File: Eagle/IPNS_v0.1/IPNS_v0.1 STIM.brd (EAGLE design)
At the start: 32.9 x 17.8 mm, 21 parts, among them J1 OUTPUT CONN, J2 POL SWITCH CONN, U1 LTC3459ES6TRMPBF, U2 LT1492CS8TRPBF

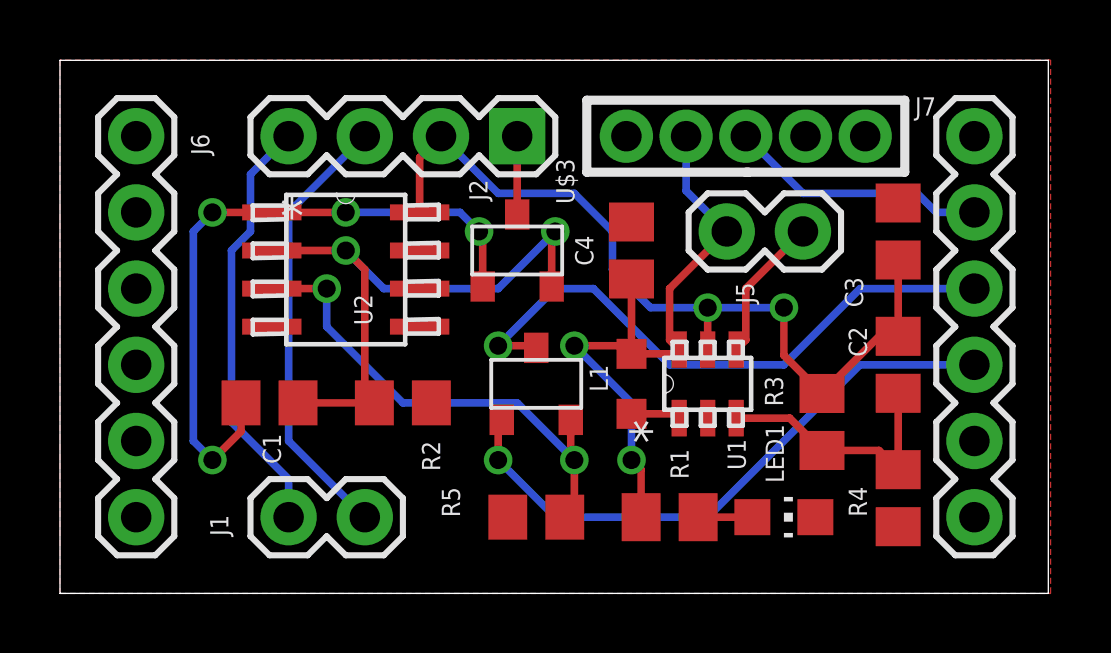
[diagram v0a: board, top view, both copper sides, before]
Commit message: Moved some components on STIM and updated Gerber files
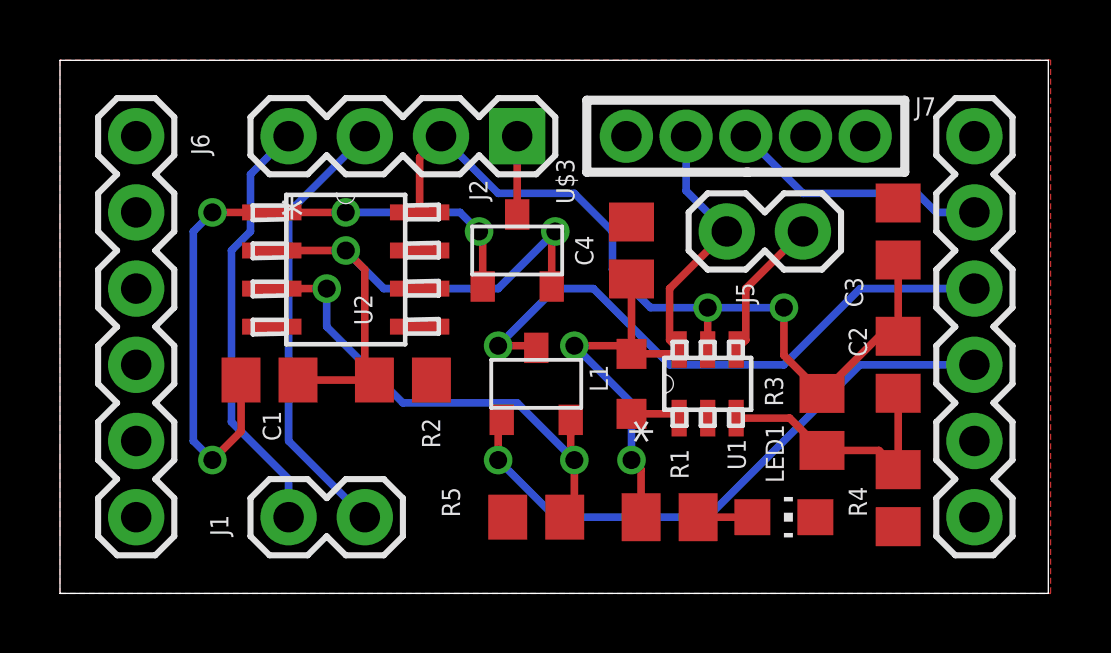
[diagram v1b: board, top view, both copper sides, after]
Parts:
- moved C1 0.76 mm to (6.99, 7.11)
- moved R2 0.76 mm to (11.4, 7.11)
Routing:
- net N$2: track 22.8 -> 23.6 mm
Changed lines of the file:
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@@
 </autorouter>
 <elements>
-<element name="C1" library="IPNS_Lib_v0.1" package="C0805" value="100pF" x="6.985" y="6.35" smashed="yes">
-<attribute name="NAME" x="7.366" y="4.318" size="0.6096" layer="25" rot="R90"/>
+<element name="C1" library="IPNS_Lib_v0.1" package="C0805" value="100pF" x="6.985" y="7.112" smashed="yes">
+<attribute name="NAME" x="7.366" y="5.08" size="0.6096" layer="25" rot="R90"/>
 </element>
 <element name="C2" library="IPNS_Lib_v0.1" package="C0805" value="47pF" x="27.94" y="7.62" smashed="yes" rot="R90">
@@
 <attribute name="NAME" x="26.162" y="10.541" size="0.6096" layer="25" rot="R270"/>
 </element>
-<element name="R2" library="IPNS_Lib_v0.1" package="R0805" value="200" x="11.43" y="6.35" smashed="yes" rot="R180">
-<attribute name="NAME" x="12.065" y="5.08" size="0.6096" layer="25" rot="R270"/>
+<element name="R2" library="IPNS_Lib_v0.1" package="R0805" value="200" x="11.43" y="7.112" smashed="yes" rot="R180">
+<attribute name="NAME" x="12.065" y="5.842" size="0.6096" layer="25" rot="R270"/>
 </element>
 <element name="R3" library="IPNS_Lib_v0.1" package="R0805" value="2Meg" x="25.4" y="5.715" smashed="yes" rot="R90">
@@
 <wire x1="10.795" y1="10.16" x2="9.525" y2="11.43" width="0.254" layer="16"/>
 <wire x1="14.605" y1="10.16" x2="10.795" y2="10.16" width="0.254" layer="16"/>
-<wire x1="7.935" y1="6.35" x2="10.48" y2="6.35" width="0.254" layer="1"/>
-<wire x1="10.48" y1="6.35" x2="10.16" y2="6.67" width="0.254" layer="1"/>
+<wire x1="7.935" y1="7.112" x2="10.48" y2="7.112" width="0.254" layer="1"/>
+<wire x1="10.48" y1="7.112" x2="10.16" y2="6.67" width="0.254" layer="1"/>
 <wire x1="10.16" y1="10.795" x2="9.525" y2="11.43" width="0.254" layer="1"/>
 <wire x1="10.16" y1="6.67" x2="10.16" y2="10.795" width="0.254" layer="1"/>
@@
 <wire x1="6.35" y1="12.7" x2="7.0612" y2="12.7" width="0.254" layer="1"/>
 <via x="5.08" y="4.445" extent="1-16" drill="0.6"/>
-<wire x1="6.035" y1="6.35" x2="6.035" y2="5.4" width="0.254" layer="1"/>
+<wire x1="6.035" y1="7.112" x2="6.035" y2="5.4" width="0.254" layer="1"/>
 <wire x1="6.035" y1="5.4" x2="5.08" y2="4.445" width="0.254" layer="1"/>
 <via x="5.08" y="12.7" extent="1-16" drill="0.6"/>
